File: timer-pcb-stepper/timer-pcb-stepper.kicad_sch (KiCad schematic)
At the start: 26 parts, among them J1 JST_05, J2 JST_05, J3 JST_05, SW5 SW_SPDT_Switch_Led_Control, SW6 SW_SPDT_Switch_Motor_1, SW7 SW_SPDT_Switch_Motor_2, SW8 SW_SPDT_Switch_Motor_3, U1 ULN2003, U3 ULN2003, U4 ULN2003

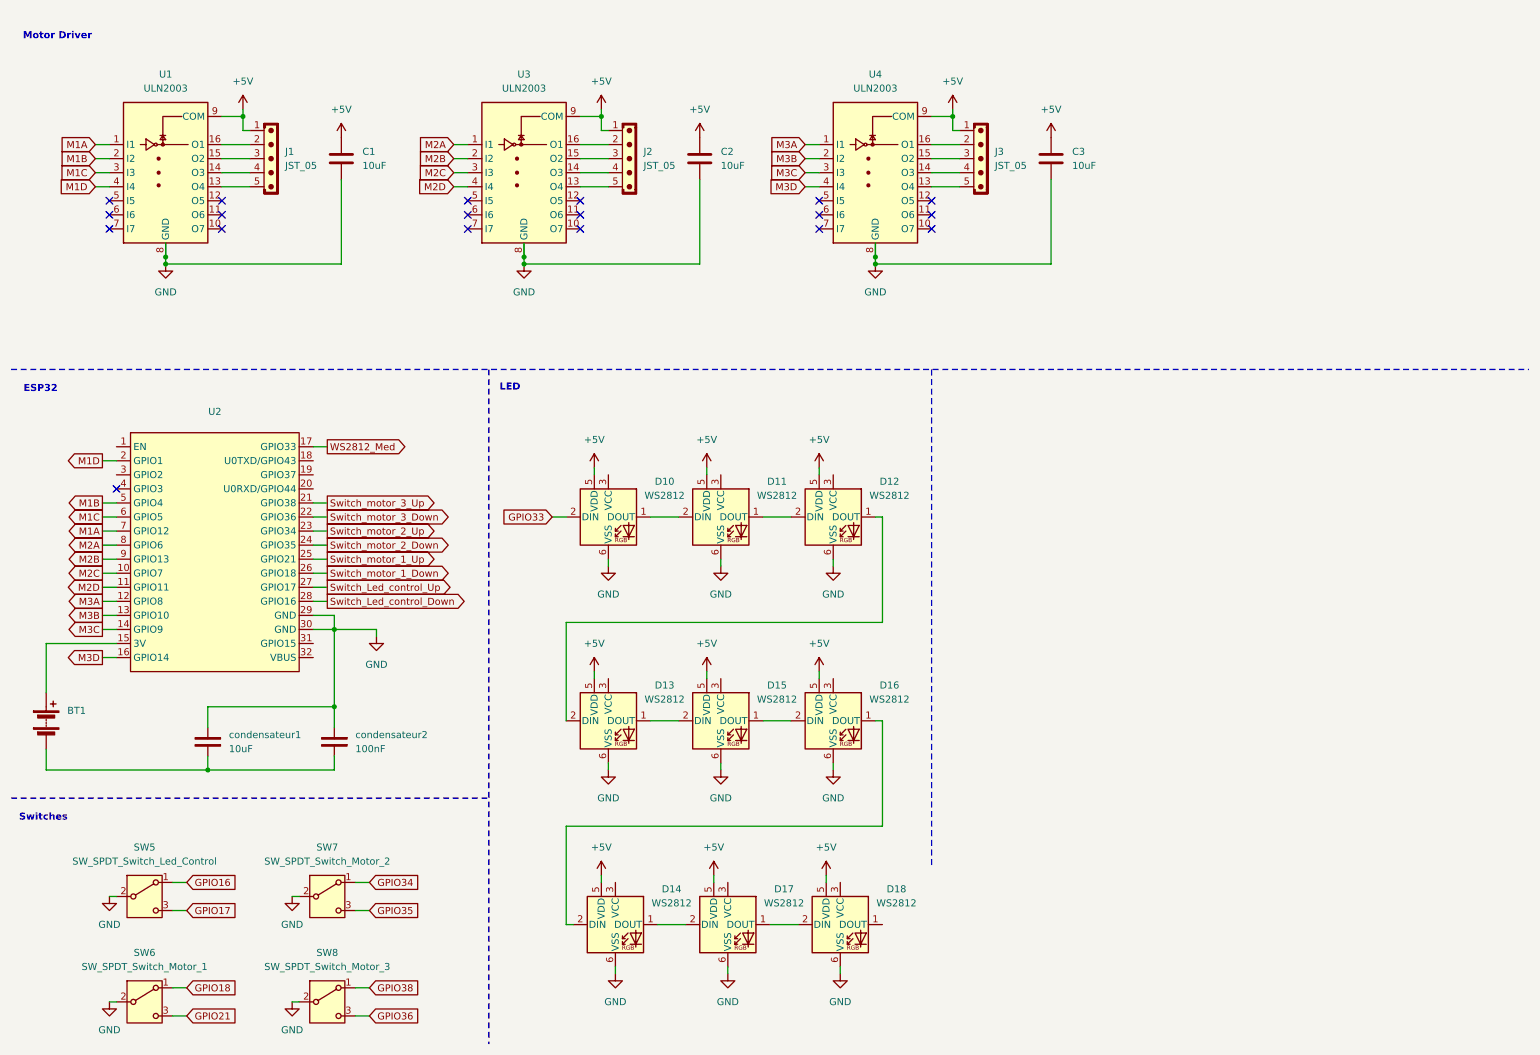
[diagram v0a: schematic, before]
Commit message: mise à jour des fichiers kicad PCB-led et PCB-stepper. circuit imprimé plus propre et ajout de connecteur jst
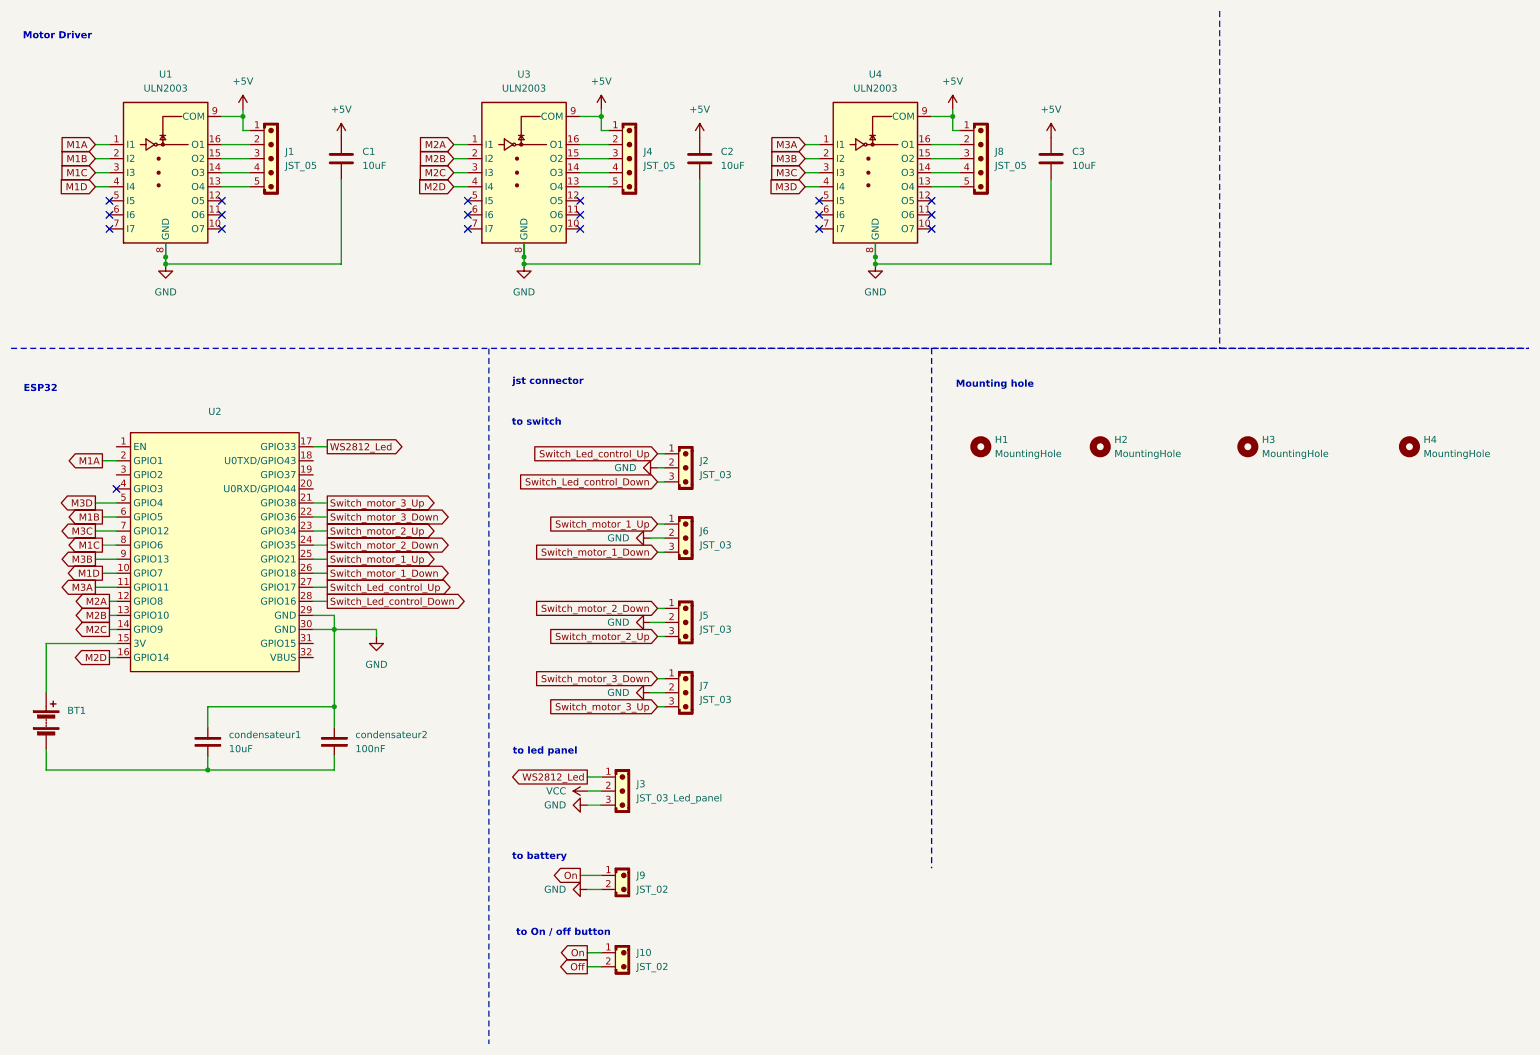
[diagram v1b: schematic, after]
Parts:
- removed D10, D11, D12, D13, D14, D15, D16, D17, D18: WS2812, LED_SMD:LED_WS2812_PLCC6_5.0x5.0mm_P1.6mm, symbol LED:WS2812
- removed SW5: SW_SPDT_Switch_Led_Control, symbol Switch:SW_SPDT
- removed SW6: SW_SPDT_Switch_Motor_1, symbol Switch:SW_SPDT
- removed SW7: SW_SPDT_Switch_Motor_2, symbol Switch:SW_SPDT
- removed SW8: SW_SPDT_Switch_Motor_3, symbol Switch:SW_SPDT
- added H1, H2, H3, H4: MountingHole, MountingHole:MountingHole_3.2mm_M3_DIN965_Pad_TopOnly, symbol Mechanical:MountingHole
- added J10, J9: JST_02, Connector_JST:JST_EH_B2B-EH-A_1x02_P2.50mm_Vertical, symbol PCM_SL_Connectors:JST_02
- added J2, J5, J6, J7: JST_03, Connector_JST:JST_XH_S3B-XH-A-1_1x03_P2.50mm_Horizontal, symbol PCM_SL_Connectors:JST_03
- added J3: JST_03_Led_panel, Connector_JST:JST_XH_S3B-XH-A-1_1x03_P2.50mm_Horizontal, symbol PCM_SL_Connectors:JST_03
- J1: JLCPCB Part # (none) -> C157991
- J4: renamed from J2; JLCPCB Part # (none) -> C157991
- J8: renamed from J3; JLCPCB Part # (none) -> C157991
- condensateur1: JLCPCB Part # (none) -> C15850
- condensateur2: JLCPCB Part # (none) -> C14663
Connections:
- net GND: now also J2.2, J3.3, J5.2, J6.2, J7.2, J9.2
- net M1A: now also U2.2 (GPIO1); no longer U2.7 (GPIO12)
- net M1B: now also U2.6 (GPIO5); no longer U2.5 (GPIO4)
- net M1C: now also U2.8 (GPIO6); no longer U2.6 (GPIO5)
- net M1D: now also U2.10 (GPIO7); no longer U2.2 (GPIO1)
- net M2A: now also U2.12 (GPIO8); no longer U2.8 (GPIO6)
- net M2B: now also U2.13 (GPIO10); no longer U2.9 (GPIO13)
- net M2C: now also U2.14 (GPIO9); no longer U2.10 (GPIO7)
- net M2D: now also U2.16 (GPIO14); no longer U2.11 (GPIO11)
- net M3A: now also U2.11 (GPIO11); no longer U2.12 (GPIO8)
- net M3B: now also U2.9 (GPIO13); no longer U2.13 (GPIO10)
- net M3C: now also U2.7 (GPIO12); no longer U2.14 (GPIO9)
- net M3D: now also U2.5 (GPIO4); no longer U2.16 (GPIO14)
- net Switch_Led_control_Down: now also J2.3
- net Switch_Led_control_Up: now also J2.1
- net Switch_motor_1_Down: now also J6.3
- net Switch_motor_1_Up: now also J6.1
- net Switch_motor_2_Down: now also J5.1
- net Switch_motor_2_Up: now also J5.3
- net Switch_motor_3_Down: now also J7.1
- net Switch_motor_3_Up: now also J7.3
- net WS2812_Med renamed WS2812_Led
- net WS2812_Led: now also J3.1
- new net Off: J10.2
- new net On: J10.1, J9.1
- new net VCC: J3.2
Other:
- note added: "Mounting hole"
- note added: "jst connector"
- note added: "to On / off button"
- note added: "to battery"
- note added: "to led panel"
- note added: "to switch"
- note removed: "LED"
- note removed: "Switches"

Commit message: mise à jour des fichiers kicad PCB-stepper. circuit imprimé plus propre et ajout de connecteur jst
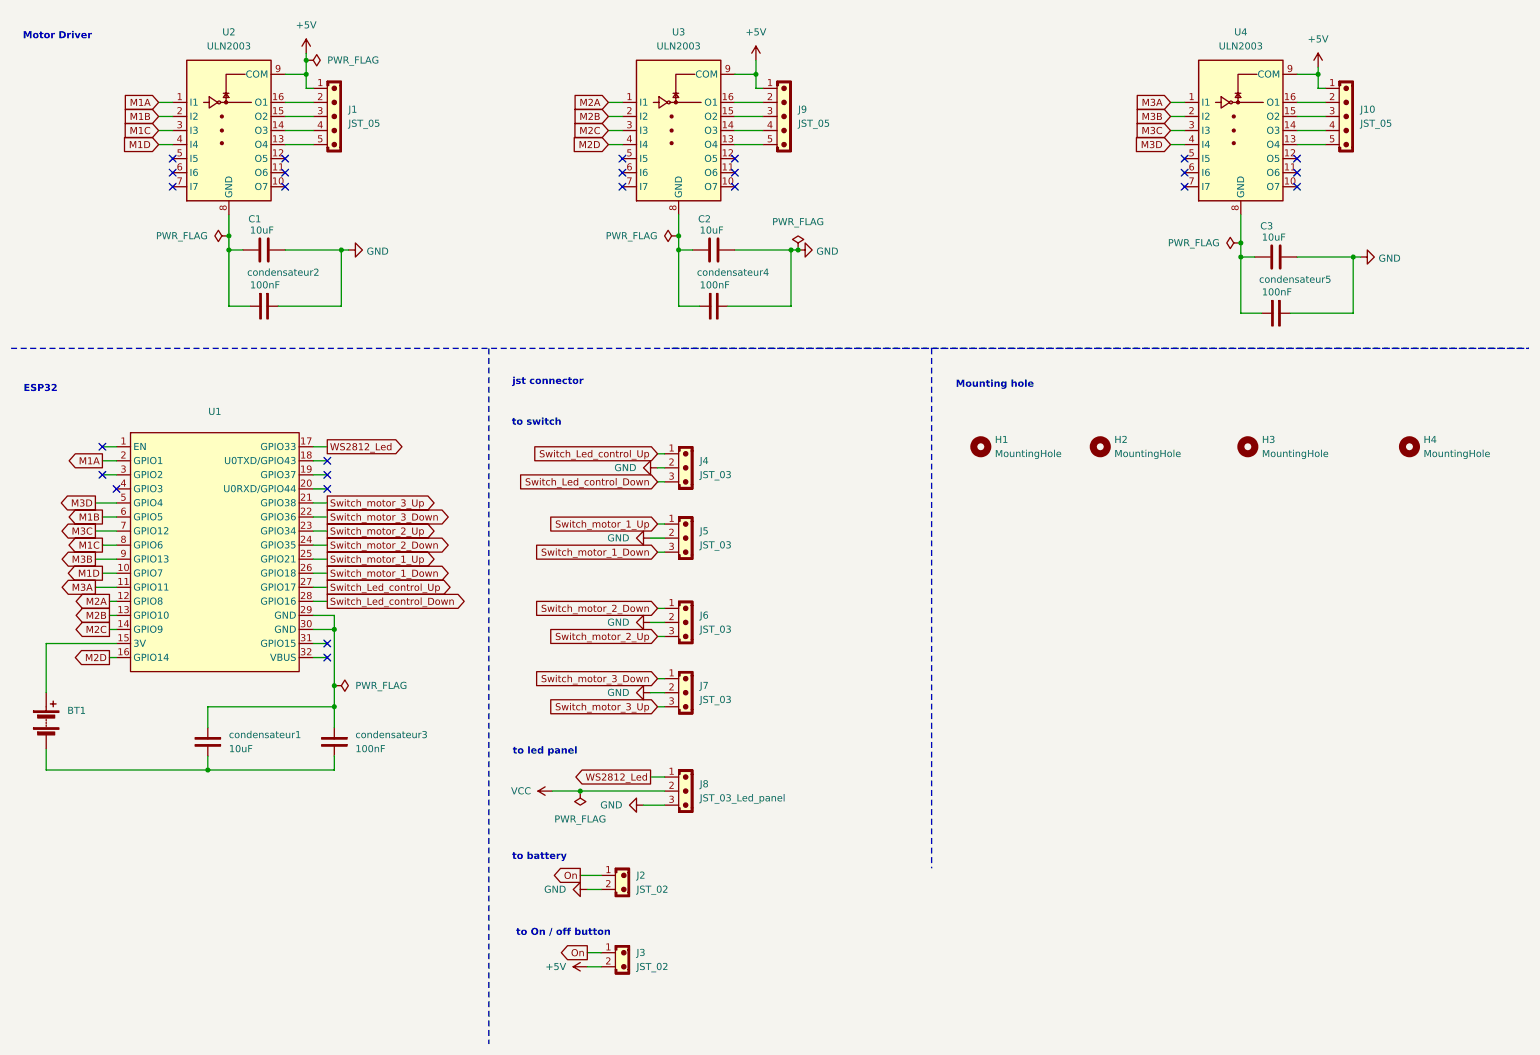
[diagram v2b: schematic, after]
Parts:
- added condensateur2, condensateur4, condensateur5: 100nF, Capacitor_THT:C_Disc_D3.0mm_W2.0mm_P2.50mm, symbol PCM_SL_Devices:Capacitor_NP
- C1, C2, C3: footprint (none) -> Capacitor_THT:C_Disc_D3.0mm_W2.0mm_P2.50mm
- renumbered J8 to J10, J9 to J2, J10 to J3, J2 to J4, J6 to J5, J5 to J6, J3 to J8, J4 to J9, U2 to U1, U1 to U2, condensateur2 to condensateur3
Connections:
- net Off is gone; now on net +5V: J3.2
- net +5V: no longer C1.1, C2.1, C3.1
- net GND: now also condensateur2.2, condensateur4.2, condensateur5.2; no longer U1.29 (GND), U1.30 (GND), U2.8 (GND), U3.8 (GND), U4.8 (GND), condensateur1.1, condensateur3.1
- new net: U1.29 (GND), U1.30 (GND), condensateur1.1, condensateur3.1
- new net: C3.1, U4.8 (GND), condensateur5.1
- new net: C2.1, U3.8 (GND), condensateur4.1
- new net: C1.1, U2.8 (GND), condensateur2.1
- no-connect marks 19 -> 26
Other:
- moved on the sheet: C2, J1, J10, J8, J9, U2, U3, U4

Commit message: rework des PCB stepper et led. création du PCB chargeur
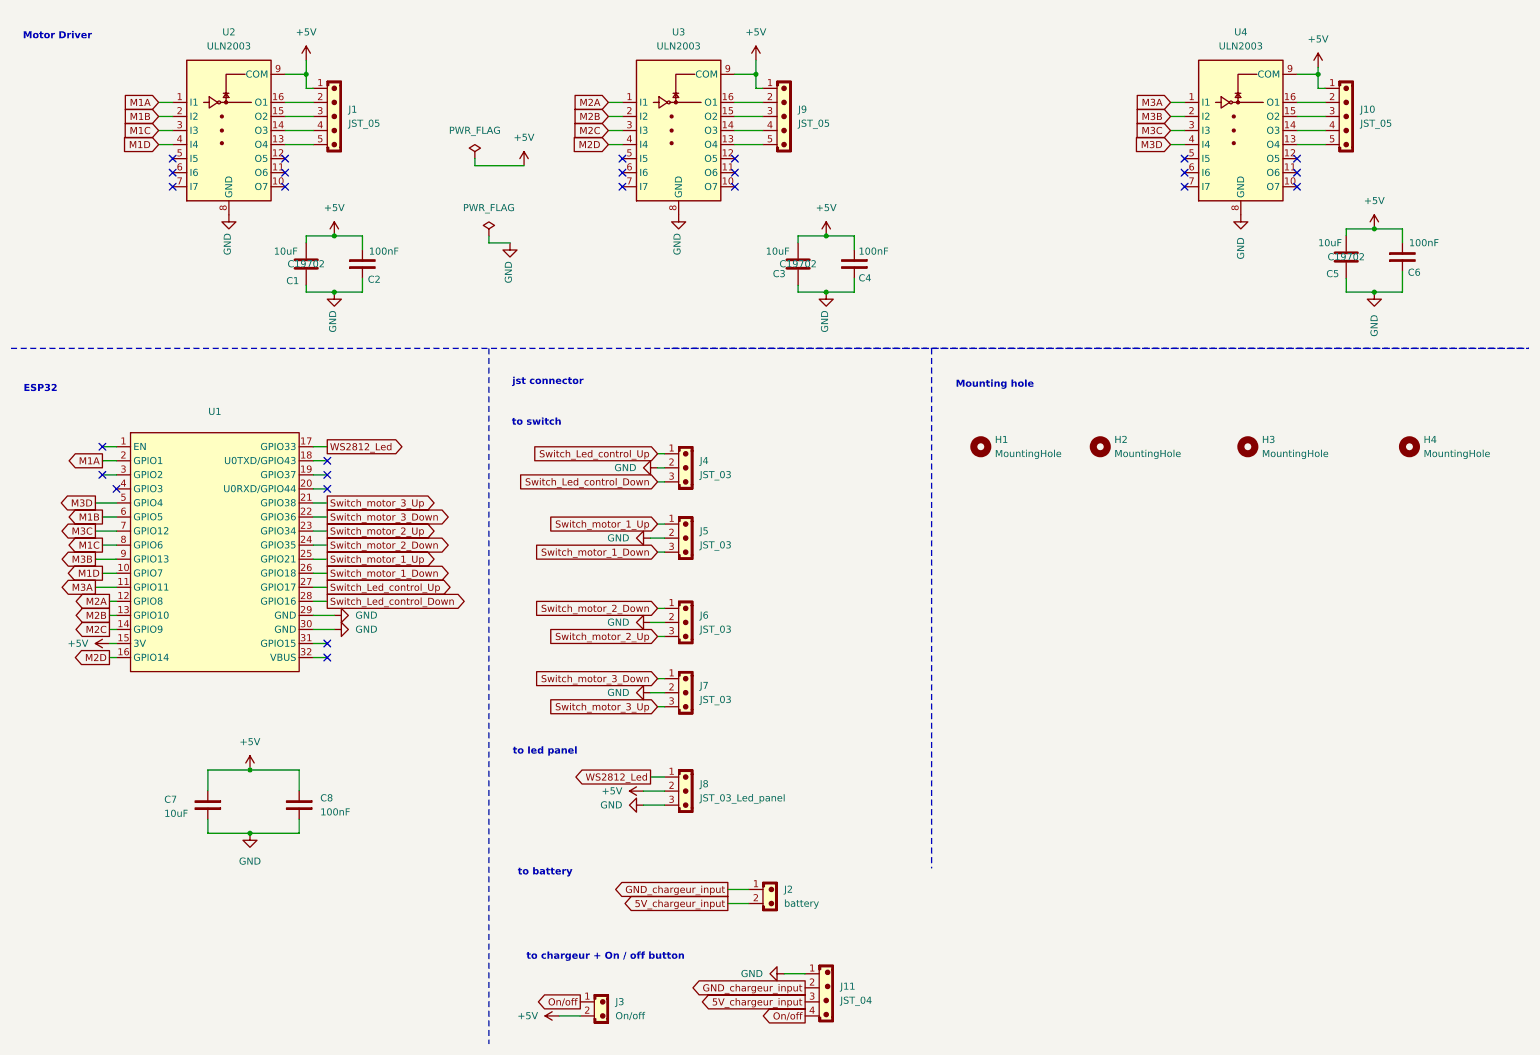
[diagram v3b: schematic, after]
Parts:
- removed BT1: Battery, symbol Device:Battery
- added J11: JST_04, Connector_JST:JST_PH_B4B-PH-K_1x04_P2.00mm_Vertical, symbol PCM_SL_Connectors:JST_04
- C1: footprint Capacitor_THT:C_Disc_D3.0mm_W2.0mm_P2.50mm -> Capacitor_SMD:C_0805_2012Metric; JLCPCB Part # (none) -> C19702
- C2: renamed from condensateur2; footprint Capacitor_THT:C_Disc_D3.0mm_W2.0mm_P2.50mm -> Capacitor_SMD:C_0603_1608Metric; JLCPCB Part # C14663 -> C1525
- C3: renamed from C2; footprint Capacitor_THT:C_Disc_D3.0mm_W2.0mm_P2.50mm -> Capacitor_SMD:C_0805_2012Metric; JLCPCB Part # (none) -> C19702
- C4: renamed from condensateur4; footprint Capacitor_THT:C_Disc_D3.0mm_W2.0mm_P2.50mm -> Capacitor_SMD:C_0603_1608Metric; JLCPCB Part # C14663 -> C1525
- C5: renamed from C3; footprint Capacitor_THT:C_Disc_D3.0mm_W2.0mm_P2.50mm -> Capacitor_SMD:C_0805_2012Metric; JLCPCB Part # (none) -> C19702
- C6: renamed from condensateur5; footprint Capacitor_THT:C_Disc_D3.0mm_W2.0mm_P2.50mm -> Capacitor_SMD:C_0603_1608Metric; JLCPCB Part # C14663 -> C1525
- C7: renamed from condensateur1; footprint Capacitor_THT:C_Disc_D3.0mm_W2.0mm_P2.50mm -> Capacitor_SMD:C_0805_2012Metric; JLCPCB Part # C15850 -> C19702
- C8: renamed from condensateur3; footprint Capacitor_THT:C_Disc_D3.0mm_W2.0mm_P2.50mm -> Capacitor_SMD:C_0603_1608Metric; JLCPCB Part # C14663 -> C1525
- J2: value JST_02 -> battery; footprint Connector_JST:JST_EH_B2B-EH-A_1x02_P2.50mm_Vertical -> Connector_JST:JST_PH_B2B-PH-K_1x02_P2.00mm_Vertical
- J3: value JST_02 -> On/off; footprint Connector_JST:JST_EH_B2B-EH-A_1x02_P2.50mm_Vertical -> Connector_JST:JST_PH_B2B-PH-K_1x02_P2.00mm_Vertical
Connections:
- net VCC is gone; now on net +5V: J8.2
- net +5V: now also C1.2, C2.2, C3.2, C4.1, C5.2, C6.2, C7.1, C8.1, U1.15 (3V)
- net GND: now also C1.1, C2.1, C3.1, C5.1, C6.1, C7.2, C8.2, U1.29 (GND), U1.30 (GND), U2.8 (GND), U3.8 (GND), U4.8 (GND), J11.1; no longer C1.2, C2.2, C3.2, C5.2, C6.2, J2.2
- net On renamed GND_chargeur_input
- net GND_chargeur_input: now also J11.2; no longer J3.1
- new net 5V_chargeur_input: J11.3, J2.2
- new net On/off: J11.4, J3.1
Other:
- note added: "to chargeur + On / off button"
- note removed: "to On / off button"
- moved on the sheet: C1, C2, C3, C4, C5, C6, C7, C8, J2
